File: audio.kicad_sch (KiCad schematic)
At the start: 10 parts, among them J4 Speaker, U7 PAM8301, U8 W25Q128JVS

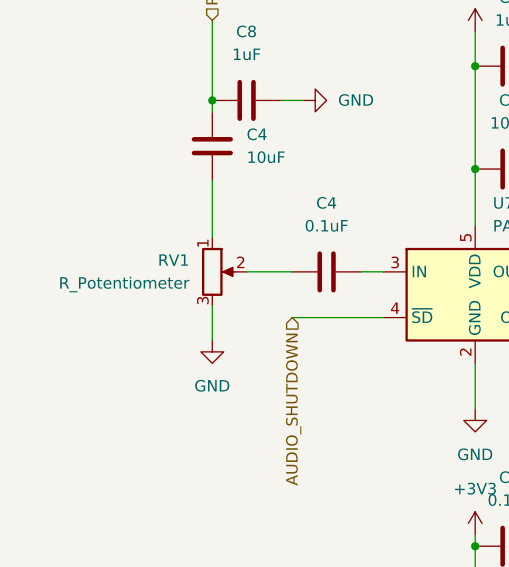
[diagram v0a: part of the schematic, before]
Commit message: Added Antenna design
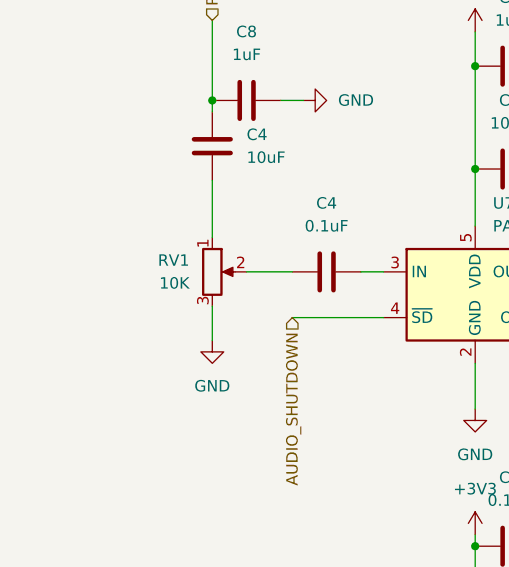
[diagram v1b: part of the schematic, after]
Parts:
- RV1: value R_Potentiometer -> 10K; footprint (none) -> Potentiometer_SMD:Potentiometer_Bourns_TC33X_Vertical; MFN (none) -> TC33X-2-103E
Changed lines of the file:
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@@
       (effects (font (size 1.27 1.27)) (justify right))
     )
-    (property "Value" "R_Potentiometer" (at 60.96 85.09 0)
+    (property "Value" "10K" (at 60.96 85.09 0)
       (effects (font (size 1.27 1.27)) (justify right))
     )
-    (property "Footprint" "" (at 63.5 83.82 0)
+    (property "Footprint" "Potentiometer_SMD:Potentiometer_Bourns_TC33X_Vertical" (at 63.5 83.82 0)
       (effects (font (size 1.27 1.27)) hide)
     )
@@
       (effects (font (size 1.27 1.27)) hide)
     )
+    (property "MFN" "TC33X-2-103E" (at 63.5 83.82 0)
+      (effects (font (size 1.27 1.27)) hide)
+    )
